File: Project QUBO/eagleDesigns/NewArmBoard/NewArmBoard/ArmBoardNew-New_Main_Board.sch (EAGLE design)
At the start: 14 parts, among them U1 BME280

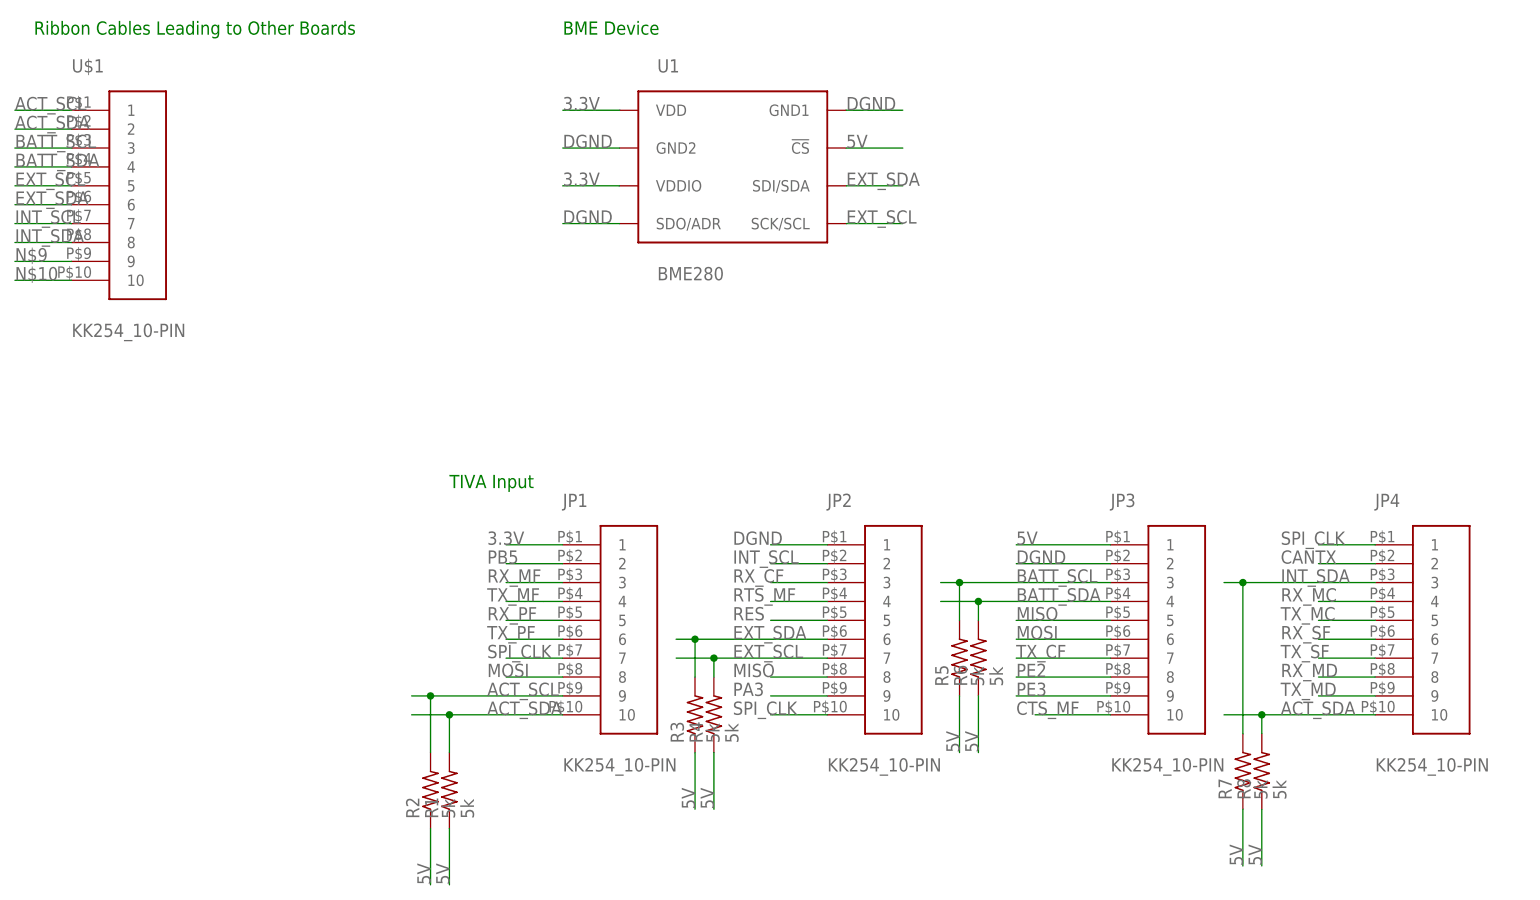
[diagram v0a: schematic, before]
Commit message: updated armboard schematic and brd layout
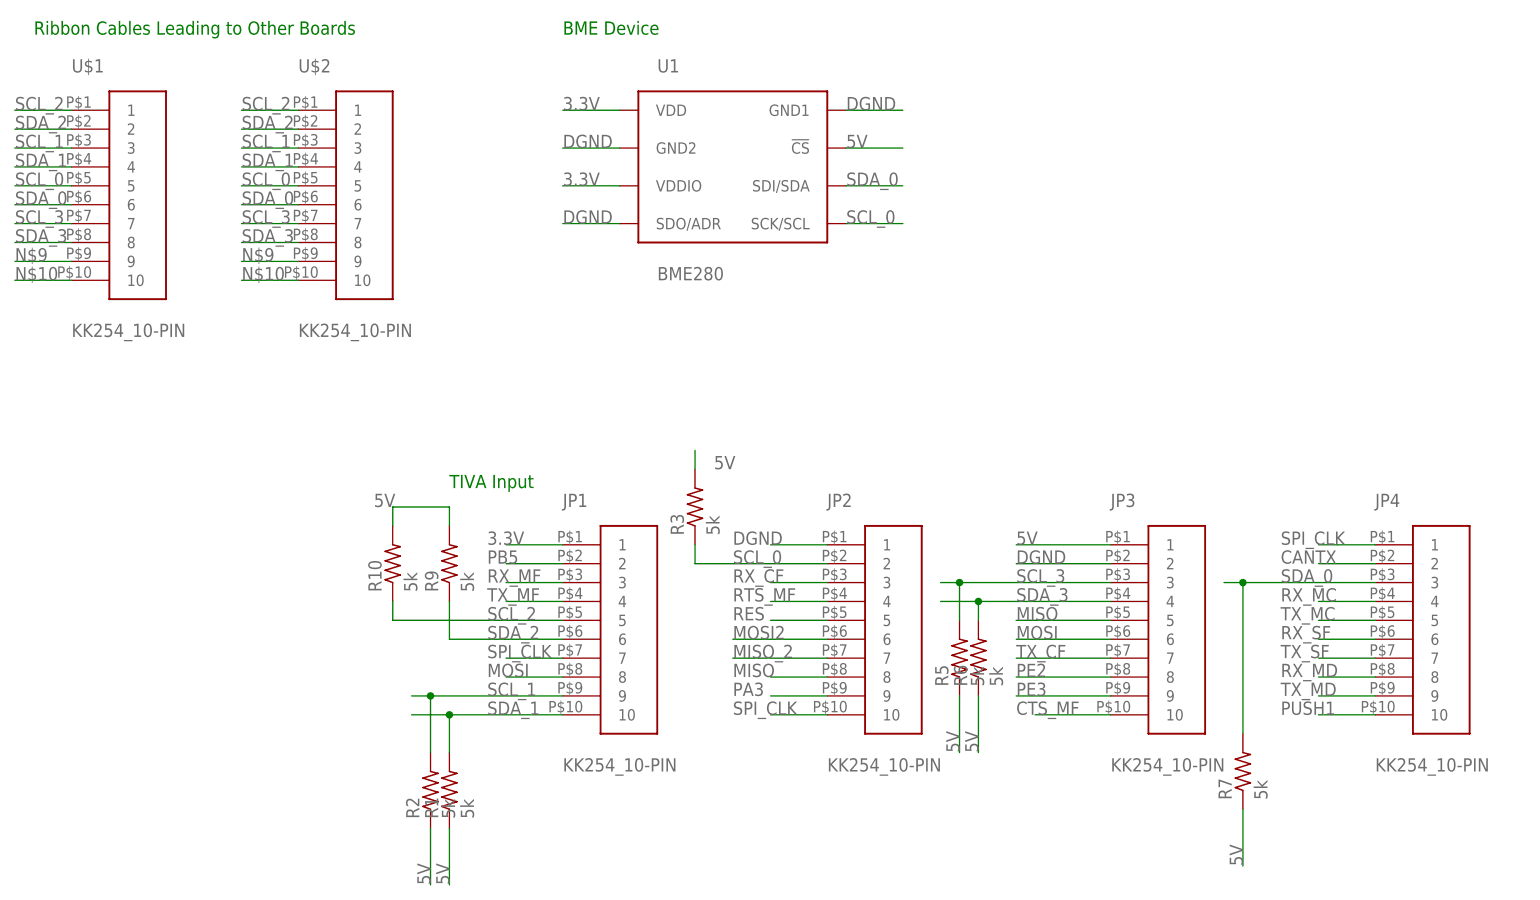
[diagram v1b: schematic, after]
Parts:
- removed R4, R8: 5k, resistor:R-US_R0805
- added R10, R9: 5k, resistor:R-US_R0805
- added U$2: KK254_10-PIN, molex:KK254_10-PIN
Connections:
- removed net ACT_SCL: JP1.9, R2.2, U$1.1
- removed net ACT_SDA: JP1.10, JP4.10, R1.2, R8.2, U$1.2
- removed net BATT_SCL: JP3.3, R5.2, U$1.3
- removed net BATT_SDA: JP3.4, R6.2, U$1.4
- removed net EXT_SCL: JP2.7, R4.2, U$1.5, U1.SCK/SCL
- removed net EXT_SDA: JP2.6, R3.2, U$1.6, U1.SDI/SDA
- removed net INT_SCL: JP2.2, U$1.7
- removed net INT_SDA: JP4.3, R7.2, U$1.8
- removed net RX_PF: JP1.5
- removed net TX_PF: JP1.6
- new net MISO_2: JP2.7
- new net MOSI2: JP2.6
- new net PUSH1: JP4.10
- new net SCL_0: JP2.2, R3.1, U$1.5, U$2.5, U1.SCK/SCL
- new net SCL_1: JP1.9, R2.2, U$1.3, U$2.3
- new net SCL_2: JP1.5, R10.1, U$1.1, U$2.1
- new net SCL_3: JP3.3, R5.2, U$1.7, U$2.7
- new net SDA_0: JP4.3, R7.2, U$1.6, U$2.6, U1.SDI/SDA
- new net SDA_1: JP1.10, R1.2, U$1.4, U$2.4
- new net SDA_2: JP1.6, R9.1, U$1.2, U$2.2
- new net SDA_3: JP3.4, R6.2, U$1.8, U$2.8
- net 5V: now also R10.2, R3.2, R9.2; no longer R3.1, R4.1, R8.1
- net N$10: now also U$2.10
- net N$9: now also U$2.9
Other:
- moved on the sheet: R3
